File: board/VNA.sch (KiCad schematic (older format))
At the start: 68 parts, among them J1 Conn_02x05_Odd_Even, J10 Conn_01x01, J11 Conn_01x01, J12 Conn_01x01, J13 Barrel_Jack, J15 Conn_02x05_Odd_Even, J17 Conn_01x04, J18 Conn_01x01, J19 Conn_01x01, J2 Conn_Coaxial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

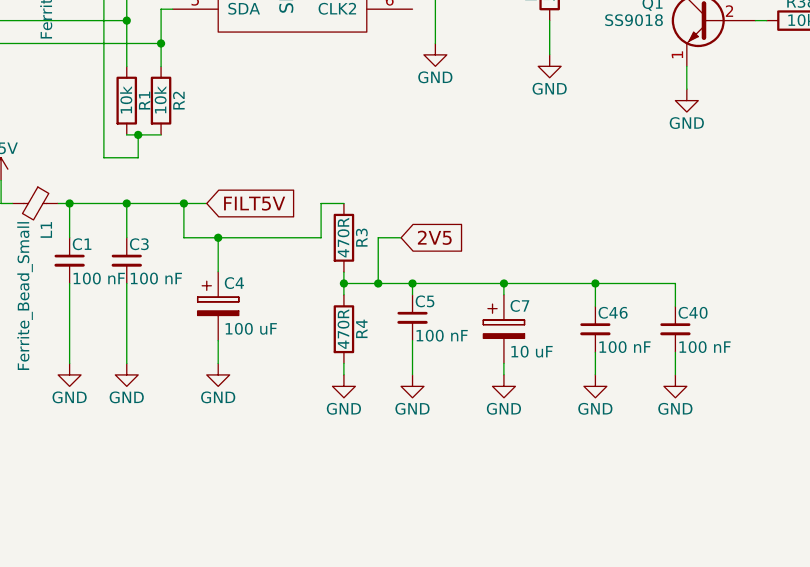
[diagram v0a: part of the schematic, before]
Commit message: Changed TL082 to LM358, other corrections to software
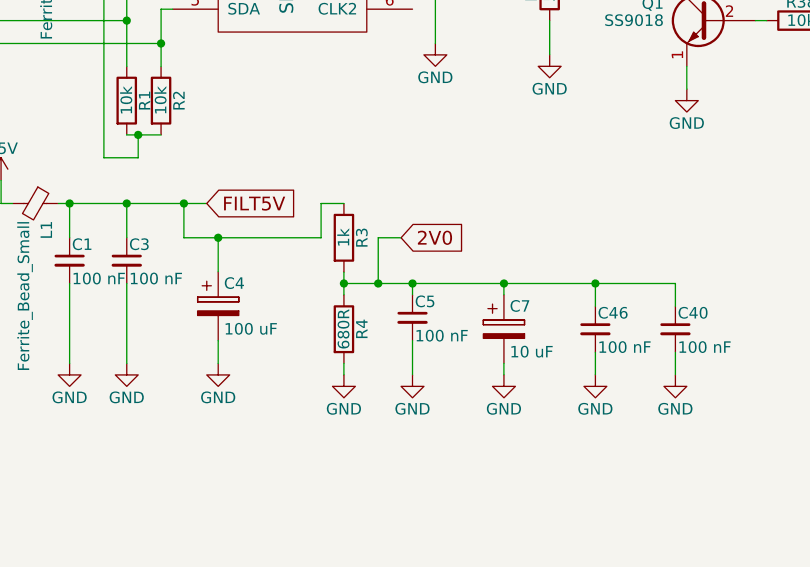
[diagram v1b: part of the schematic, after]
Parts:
- R3: value 470R -> 1k
- R4: value 470R -> 680R
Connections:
- net 2V5 renamed 2V0
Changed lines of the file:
@@
 P 2550 6250
 F 0 "R3" V 2630 6250 50  0000 C CNN
-F 1 "470R" V 2550 6250 50  0000 C CNN
+F 1 "1k" V 2550 6250 50  0000 C CNN
 F 2 "Resistors_THT:R_Axial_DIN0207_L6.3mm_D2.5mm_P7.62mm_Horizontal" V 2480 6250 50  0001 C CNN
 F 3 "" H 2550 6250 50  0001 C CNN
@@
 P 2550 6650
 F 0 "R4" V 2630 6650 50  0000 C CNN
-F 1 "470R" V 2550 6650 50  0000 C CNN
+F 1 "680R" V 2550 6650 50  0000 C CNN
 F 2 "Resistors_THT:R_Axial_DIN0207_L6.3mm_D2.5mm_P7.62mm_Horizontal" V 2480 6650 50  0001 C CNN
 F 3 "" H 2550 6650 50  0001 C CNN
@@
 $EndComp
 Text GLabel 2800 6250 2    60   Input ~ 0
-2V5
+2V0
 $Comp
 L CP C4

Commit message: A few minor fixes, grounding, etc.
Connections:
- net GND: now also J18.1 (Pin_1), J19.1 (Pin_1), J20.1 (Pin_1), J21.1 (Pin_1)
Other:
- moved on the sheet: J18, J19, J20, J21
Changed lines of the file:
@@
 L Conn_01x01 J18
 U 1 1 5BB293CD
-P 950 3300
-F 0 "J18" H 950 3400 50  0000 C CNN
-F 1 "Conn_01x01" H 950 3200 50  0000 C CNN
-F 2 "Connectors:1pin" H 950 3300 50  0001 C CNN
-F 3 "" H 950 3300 50  0001 C CNN
-	1    950  3300
+P 700 3600
+F 0 "J18" H 700 3700 50  0000 C CNN
+F 1 "Conn_01x01" H 700 3500 50  0000 C CNN
+F 2 "Connectors:1pin" H 700 3600 50  0001 C CNN
+F 3 "" H 700 3600 50  0001 C CNN
+	1    700  3600
 	-1   0    0    1
 $EndComp
@@
 L Conn_01x01 J19
 U 1 1 5BB2949B
-P 950 3600
-F 0 "J19" H 950 3700 50  0000 C CNN
-F 1 "Conn_01x01" H 950 3500 50  0000 C CNN
-F 2 "Connectors:1pin" H 950 3600 50  0001 C CNN
-F 3 "" H 950 3600 50  0001 C CNN
-	1    950  3600
+P 700 3900
+F 0 "J19" H 700 4000 50  0000 C CNN
+F 1 "Conn_01x01" H 700 3800 50  0000 C CNN
+F 2 "Connectors:1pin" H 700 3900 50  0001 C CNN
+F 3 "" H 700 3900 50  0001 C CNN
+	1    700  3900
 	-1   0    0    1
 $EndComp
@@
 L Conn_01x01 J20
 U 1 1 5BB29562
-P 1500 3300
-F 0 "J20" H 1500 3400 50  0000 C CNN
-F 1 "Conn_01x01" H 1500 3200 50  0000 C CNN
-F 2 "Connectors:1pin" H 1500 3300 50  0001 C CNN
-F 3 "" H 1500 3300 50  0001 C CNN
-	1    1500 3300
+P 1250 3600
+F 0 "J20" H 1250 3700 50  0000 C CNN
+F 1 "Conn_01x01" H 1250 3500 50  0000 C CNN
+F 2 "Connectors:1pin" H 1250 3600 50  0001 C CNN
+F 3 "" H 1250 3600 50  0001 C CNN
+	1    1250 3600
 	-1   0    0    1
 $EndComp
@@
 L Conn_01x01 J21
 U 1 1 5BB29632
-P 1500 3600
-F 0 "J21" H 1500 3700 50  0000 C CNN
-F 1 "Conn_01x01" H 1500 3500 50  0000 C CNN
-F 2 "Connectors:1pin" H 1500 3600 50  0001 C CNN
-F 3 "" H 1500 3600 50  0001 C CNN
-	1    1500 3600
+P 1250 3900
+F 0 "J21" H 1250 4000 50  0000 C CNN
+F 1 "Conn_01x01" H 1250 3800 50  0000 C CNN
+F 2 "Connectors:1pin" H 1250 3900 50  0001 C CNN
+F 3 "" H 1250 3900 50  0001 C CNN
+	1    1250 3900
 	-1   0    0    1
 $EndComp
@@
 Wire Wire Line
 	10900 3750 10850 3750
+$Comp
+L GND #PWR?
+U 1 1 5C206F60
+P 1500 3600
+F 0 "#PWR?" H 1500 3350 50  0001 C CNN
+F 1 "GND" H 1500 3450 50  0000 C CNN
+F 2 "" H 1500 3600 50  0001 C CNN
+F 3 "" H 1500 3600 50  0001 C CNN
+	1    1500 3600
+	1    0    0    -1
+$EndComp
+Wire Wire Line
+	1450 3600 1500 3600
+$Comp
+L GND #PWR?
+U 1 1 5C2071AB
+P 1500 3900
+F 0 "#PWR?" H 1500 3650 50  0001 C CNN
+F 1 "GND" H 1500 3750 50  0000 C CNN
+F 2 "" H 1500 3900 50  0001 C CNN
+F 3 "" H 1500 3900 50  0001 C CNN
+	1    1500 3900
+	1    0    0    -1
+$EndComp
+Wire Wire Line
+	1450 3900 1500 3900
+$Comp
+L GND #PWR?
+U 1 1 5C2073B3
+P 950 3900
+F 0 "#PWR?" H 950 3650 50  0001 C CNN
+F 1 "GND" H 950 3750 50  0000 C CNN
+F 2 "" H 950 3900 50  0001 C CNN
+F 3 "" H 950 3900 50  0001 C CNN
+	1    950  3900
+	1    0    0    -1
+$EndComp
+Wire Wire Line
+	900  3900 950  3900
+$Comp
+L GND #PWR?
+U 1 1 5C2075BC
+P 950 3600
+F 0 "#PWR?" H 950 3350 50  0001 C CNN
+F 1 "GND" H 950 3450 50  0000 C CNN
+F 2 "" H 950 3600 50  0001 C CNN
+F 3 "" H 950 3600 50  0001 C CNN
+	1    950  3600
+	1    0    0    -1
+$EndComp
+Wire Wire Line
+	900  3600 950  3600
 $EndSCHEMATC

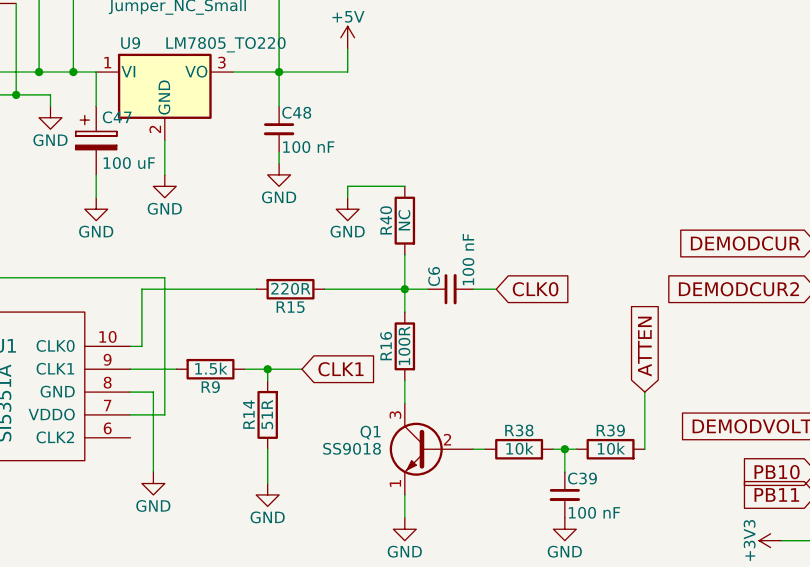
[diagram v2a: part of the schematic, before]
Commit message: Added attenuation option to touchscreen, fixed attenuation resistors
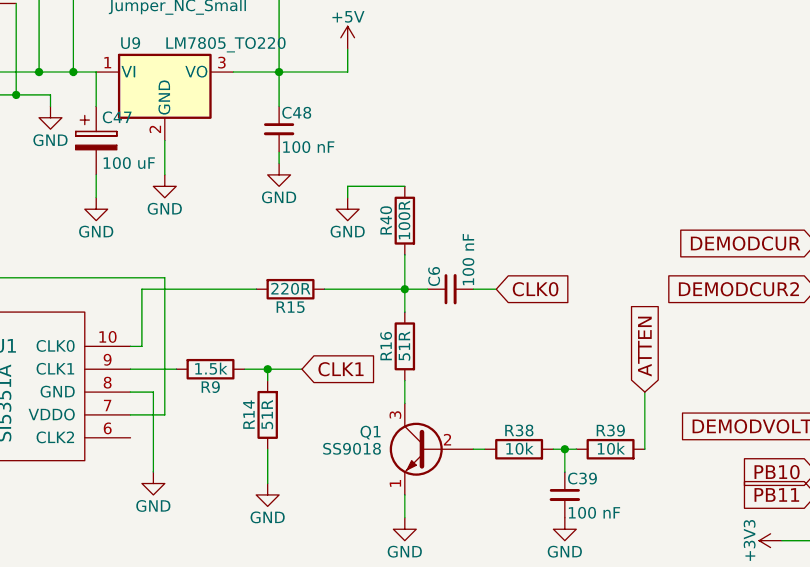
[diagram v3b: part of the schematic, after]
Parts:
- R16: value 100R -> 51R
- R40: value NC -> 100R
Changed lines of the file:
@@
 P 4050 4850
 F 0 "R16" V 4130 4850 50  0000 C CNN
-F 1 "100R" V 4050 4850 50  0000 C CNN
+F 1 "51R" V 4050 4850 50  0000 C CNN
 F 2 "Resistors_THT:R_Axial_DIN0207_L6.3mm_D2.5mm_P7.62mm_Horizontal" V 3980 4850 50  0001 C CNN
 F 3 "" H 4050 4850 50  0001 C CNN
@@
 P 4050 4300
 F 0 "R40" V 4130 4300 50  0000 C CNN
-F 1 "NC" V 4050 4300 50  0000 C CNN
+F 1 "100R" V 4050 4300 50  0000 C CNN
 F 2 "Resistors_THT:R_Axial_DIN0207_L6.3mm_D2.5mm_P7.62mm_Horizontal" V 3980 4300 50  0001 C CNN
 F 3 "" H 4050 4300 50  0001 C CNN

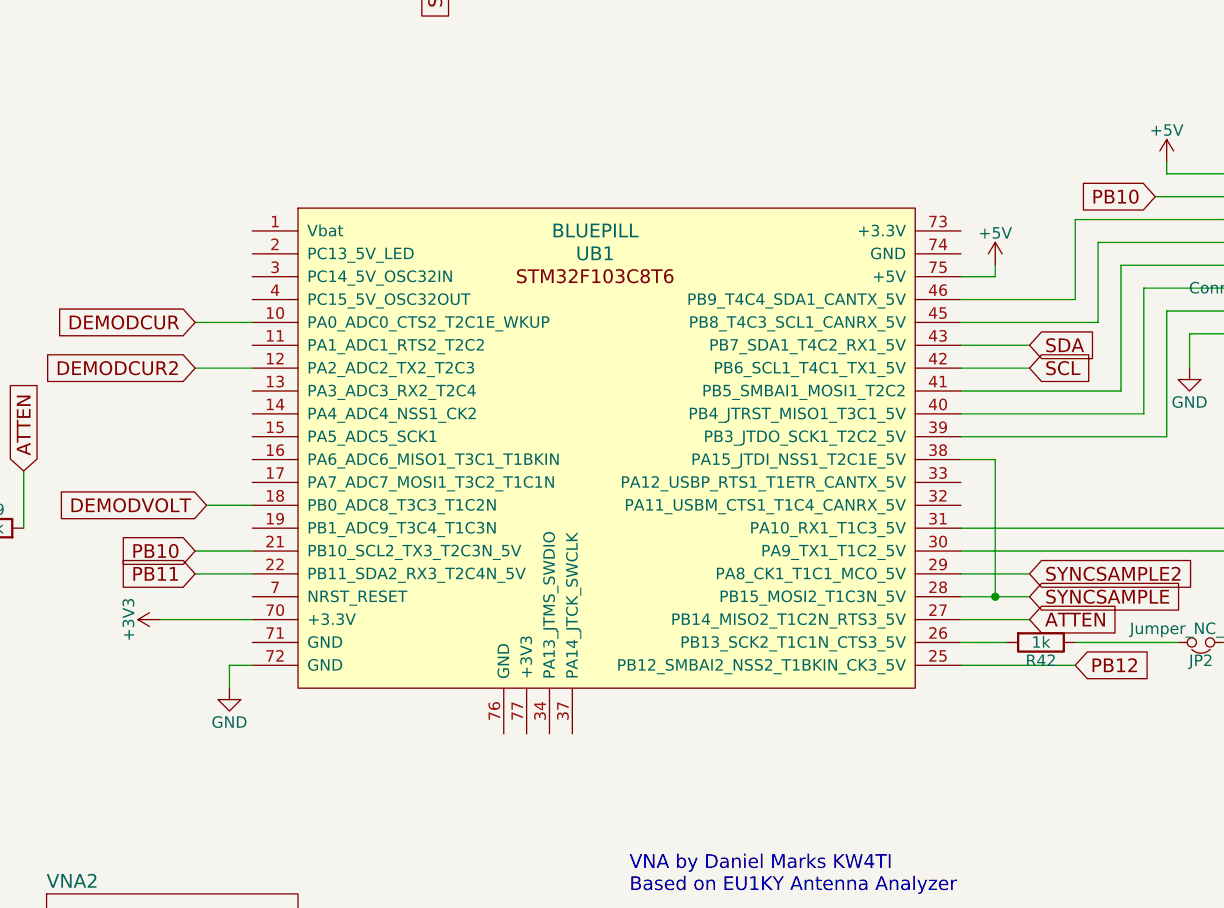
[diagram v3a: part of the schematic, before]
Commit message: Added ground connections
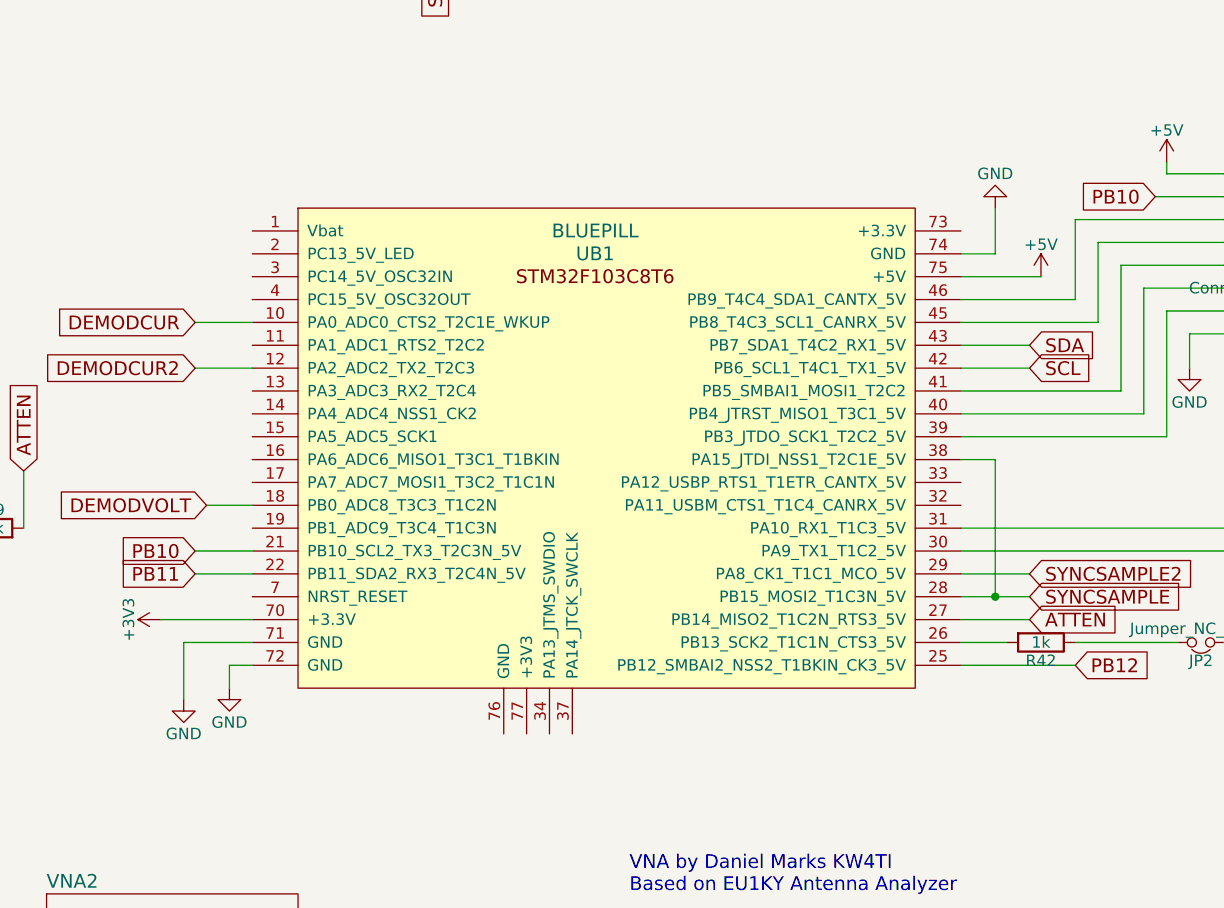
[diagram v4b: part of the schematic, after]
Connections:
- net GND: now also UB1.71 (GND), UB1.74 (GND)
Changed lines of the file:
@@
 L +5V #PWR30
 U 1 1 5BB2CE22
-P 9350 4150
-F 0 "#PWR30" H 9350 4000 50  0001 C CNN
-F 1 "+5V" H 9350 4290 50  0000 C CNN
-F 2 "" H 9350 4150 50  0001 C CNN
-F 3 "" H 9350 4150 50  0001 C CNN
-	1    9350 4150
+P 9550 4200
+F 0 "#PWR30" H 9550 4050 50  0001 C CNN
+F 1 "+5V" H 9550 4340 50  0000 C CNN
+F 2 "" H 9550 4200 50  0001 C CNN
+F 3 "" H 9550 4200 50  0001 C CNN
+	1    9550 4200
 	1    0    0    -1
 $EndComp
@@
 	6000 6000 6000 5900
 Wire Wire Line
-	9350 4200 9200 4200
-Wire Wire Line
-	9350 4150 9350 4200
+	9200 4200 9550 4200
 Wire Wire Line
 	5850 4400 6100 4400
@@
 Wire Wire Line
 	900  3600 950  3600
+Wire Wire Line
+	9200 4100 9350 4100
+Wire Wire Line
+	9350 4100 9350 3900
+$Comp
+L GND #PWR?
+U 1 1 5C258D29
+P 9350 3900
+F 0 "#PWR?" H 9350 3650 50  0001 C CNN
+F 1 "GND" H 9350 3750 50  0000 C CNN
+F 2 "" H 9350 3900 50  0001 C CNN
+F 3 "" H 9350 3900 50  0001 C CNN
+	1    9350 3900
+	-1   0    0    1
+$EndComp
+$Comp
+L GND #PWR?
+U 1 1 5C25906A
+P 5800 6050
+F 0 "#PWR?" H 5800 5800 50  0001 C CNN
+F 1 "GND" H 5800 5900 50  0000 C CNN
+F 2 "" H 5800 6050 50  0001 C CNN
+F 3 "" H 5800 6050 50  0001 C CNN
+	1    5800 6050
+	1    0    0    -1
+$EndComp
+Wire Wire Line
+	5800 6050 5800 5800
+Wire Wire Line
+	5800 5800 6100 5800
 $EndSCHEMATC

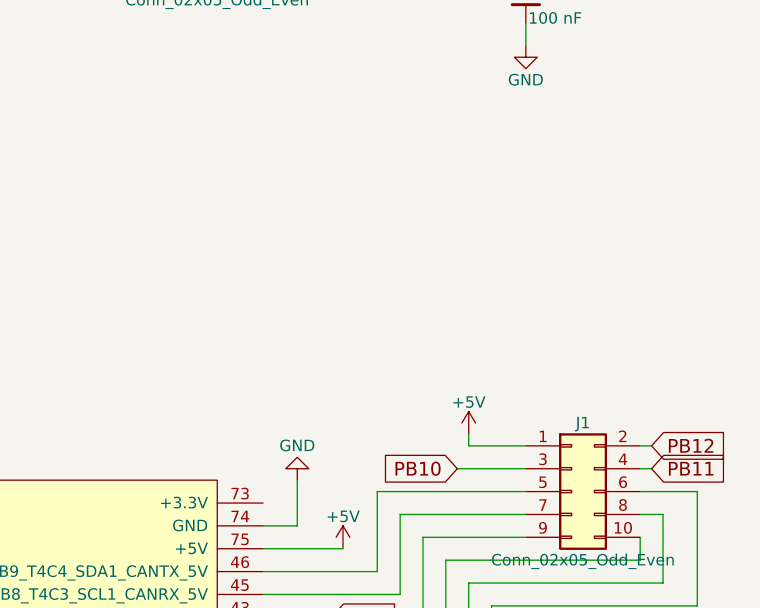
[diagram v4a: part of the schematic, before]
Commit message: Changed SMA connector, added dual power option for LCD
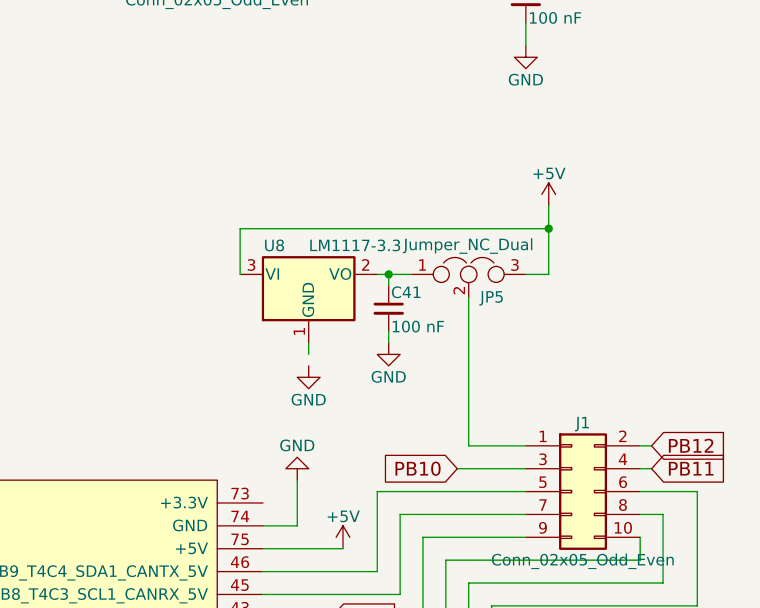
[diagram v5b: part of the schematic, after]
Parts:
- added C41: 100 nF, Capacitors_THT:C_Disc_D5.0mm_W2.5mm_P2.50mm, symbol C_Small
- added JP5: Jumper_NC_Dual, Pin_Headers:Pin_Header_Straight_1x03_Pitch2.54mm, symbol Jumper_NC_Dual
- added U8: LM1117-3.3, TO_SOT_Packages_THT:TO-220-3_Vertical, symbol LM1117-3.3
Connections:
- net +5V: now also JP5.3, U8.3 (VI); no longer J1.1 (Pin_1)
- net GND: now also C41.2
- new net: J1.1 (Pin_1), JP5.2
- new net: C41.1, JP5.1, U8.2 (VO)

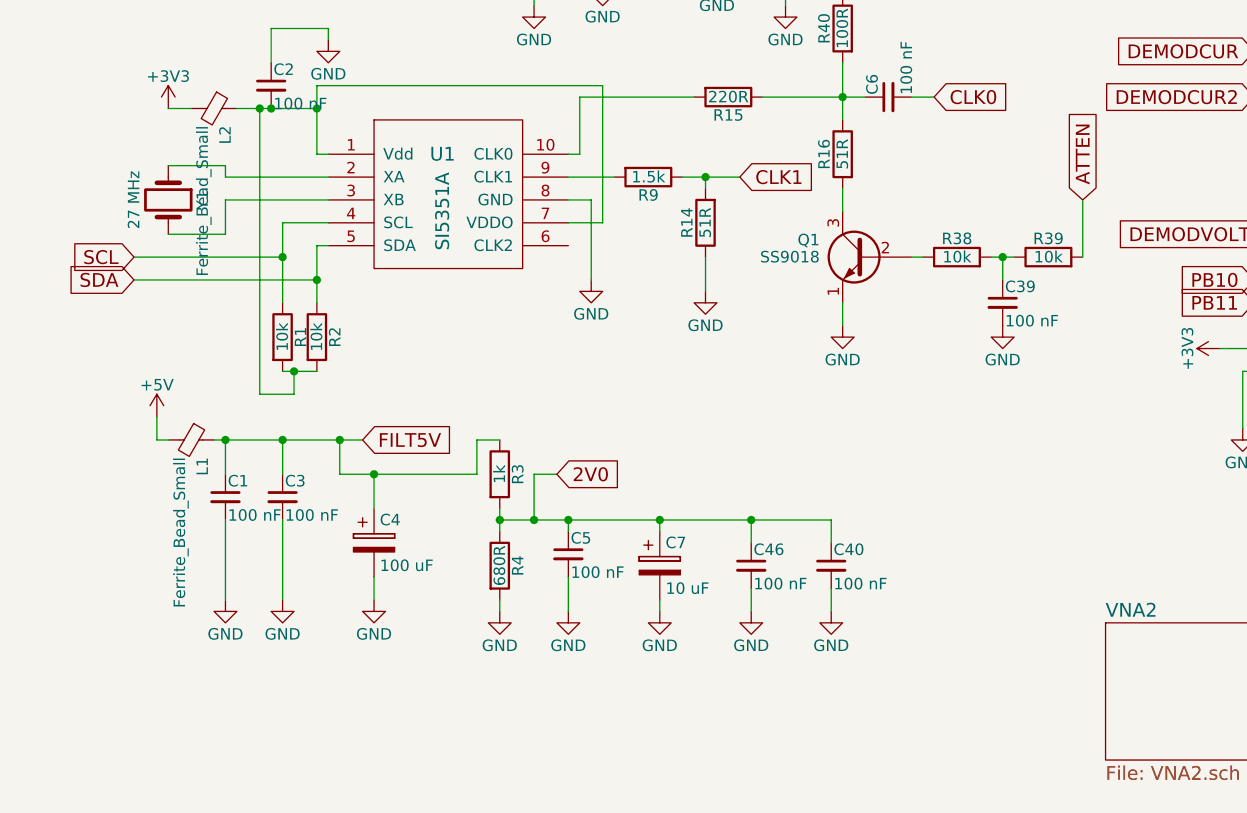
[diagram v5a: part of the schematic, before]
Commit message: Increased isolation between ports
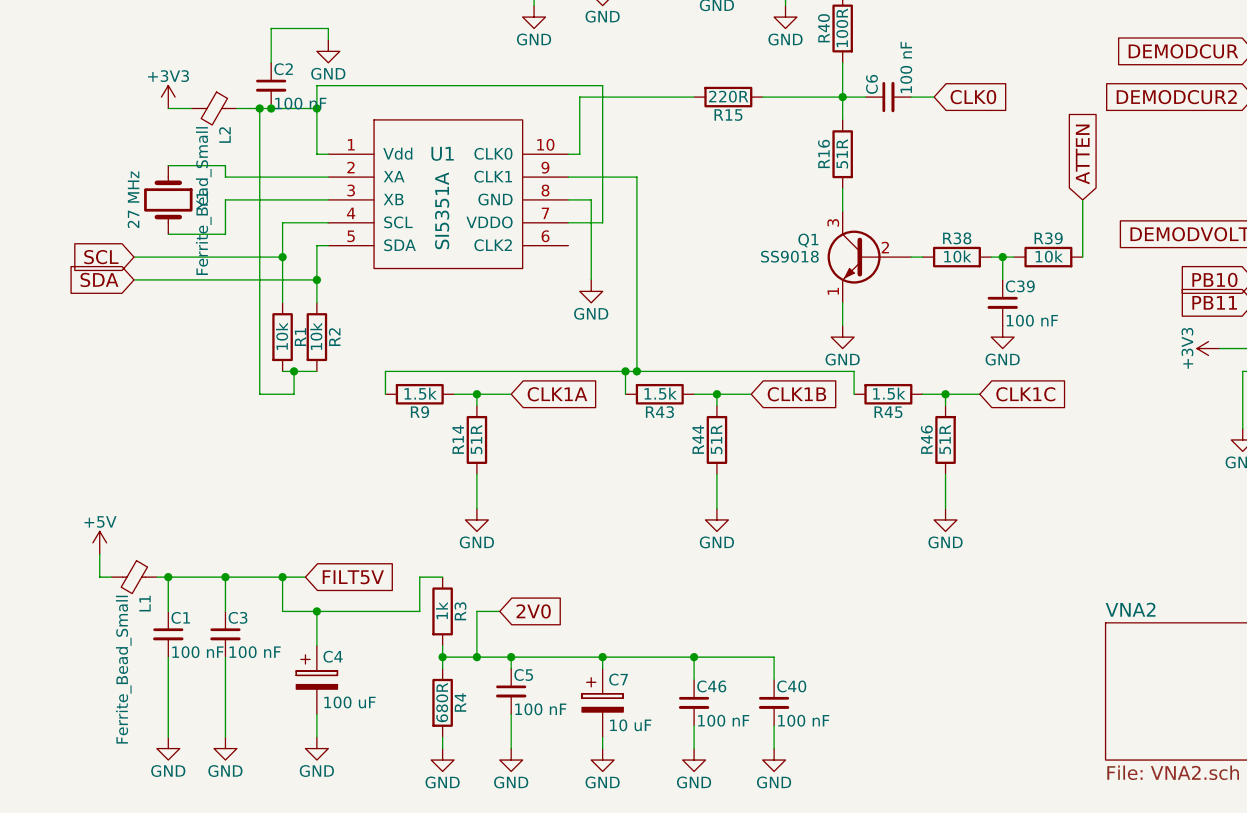
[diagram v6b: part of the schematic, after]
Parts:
- added R43, R45: 1.5k, Resistors_THT:R_Axial_DIN0207_L6.3mm_D2.5mm_P7.62mm_Horizontal, symbol R
- added R44, R46: 51R, Resistors_THT:R_Axial_DIN0207_L6.3mm_D2.5mm_P7.62mm_Horizontal, symbol R
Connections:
- net GND: now also R44.1, R46.1
- net at R9.2, U1.9 (CLK1): now also R43.2, R45.2
- net CLK1 renamed CLK1A
- new net CLK1B: R43.1, R44.2
- new net CLK1C: R45.1, R46.2
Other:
- moved on the sheet: C1, C3, C4, C40, C46, C5, C7, L1, R14, R3, R4, R9
